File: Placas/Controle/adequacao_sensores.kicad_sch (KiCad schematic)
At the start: 2 parts, among them U1 LM324

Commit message: Adição de circuitos opcionais para PWM
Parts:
- C1: footprint Capacitor_THT:C_Disc_D8.0mm_W5.0mm_P7.50mm -> Capacitor_SMD:C_0805_2012Metric_Pad1.18x1.45mm_HandSolder
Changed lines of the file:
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@@
 		(dnp no)
 		(fields_autoplaced yes)
-		(property "Reference" "#PWR9"
+		(property "Reference" "#PWR11"
 			(at 184.15 49.53 0)
 			(effects
@@
 			(project "board"
 				(path "/01568b53-f202-4f02-9c1a-9c10c7610b4b/64ed1ee1-6201-4cd1-840c-b46b599d55ab"
-					(reference "#PWR9")
+					(reference "#PWR11")
 					(unit 1)
 				)
@@
 			)
 		)
-		(property "Footprint" "Capacitor_THT:C_Disc_D8.0mm_W5.0mm_P7.50mm"
+		(property "Footprint" "Capacitor_SMD:C_0805_2012Metric_Pad1.18x1.45mm_HandSolder"
 			(at 199.0852 49.53 0)
 			(effects
@@
 		(dnp no)
 		(fields_autoplaced yes)
-		(property "Reference" "#PWR8"
+		(property "Reference" "#PWR10"
 			(at 184.15 41.91 0)
 			(effects
@@
 			(project "board"
 				(path "/01568b53-f202-4f02-9c1a-9c10c7610b4b/64ed1ee1-6201-4cd1-840c-b46b599d55ab"
-					(reference "#PWR8")
+					(reference "#PWR10")
 					(unit 1)
 				)
@@
 			)
 		)
-		(property "C_sensor" "0,1u"
+		(property "C_sensor_1" "0,1u"
+			(at 41.91 50.8 0)
+			(effects
+				(font
+					(size 1.27 1.27)
+				)
+				(hide yes)
+			)
+		)
+		(property "C_sensor_2" "4,7u"
 			(at 41.91 50.8 0)
 			(effects
@@
 			)
 		)
-		(property "C_sensor" "0,1u"
+		(property "C_sensor_1" "0,1u"
 			(at 41.91 21.59 0)
 			(effects
+				(font
+					(size 1.27 1.27)
+				)
+				(hide yes)
+			)
+		)
+		(property "C_sensor_2" "4,7u"
+			(at 41.91 21.59 0)
+			(effects

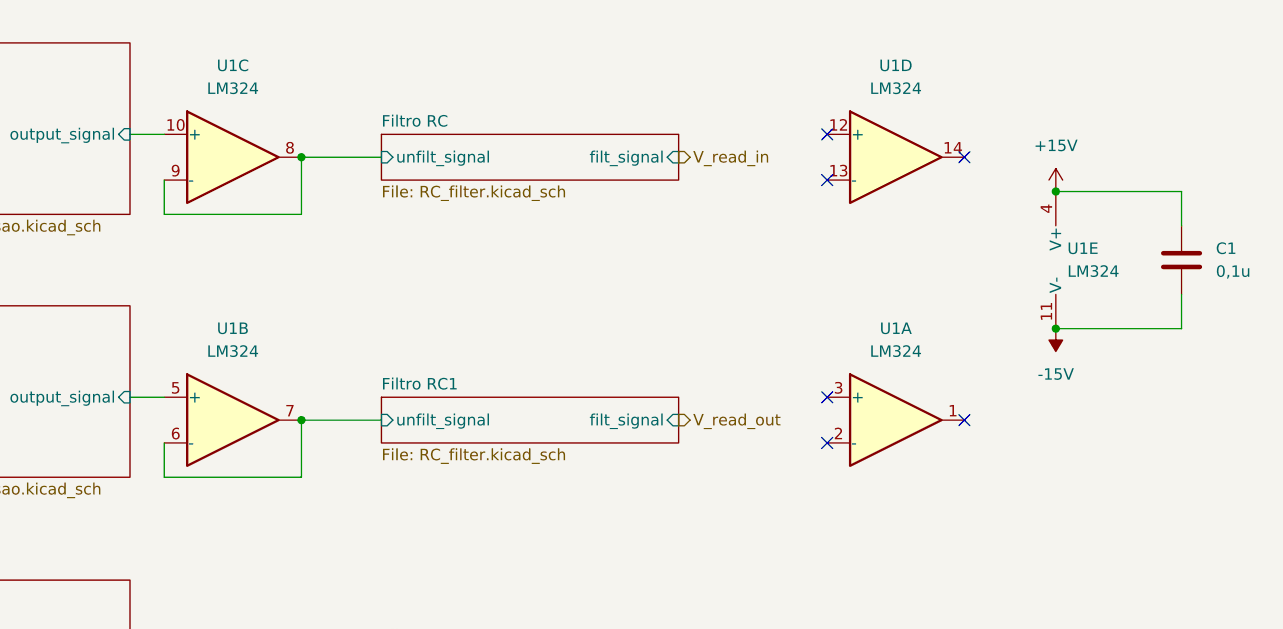
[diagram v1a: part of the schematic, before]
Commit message: Modificações nas duas placas, adição de furos para montagem, melhora na posição dos micros e conectores para comunicação SPI
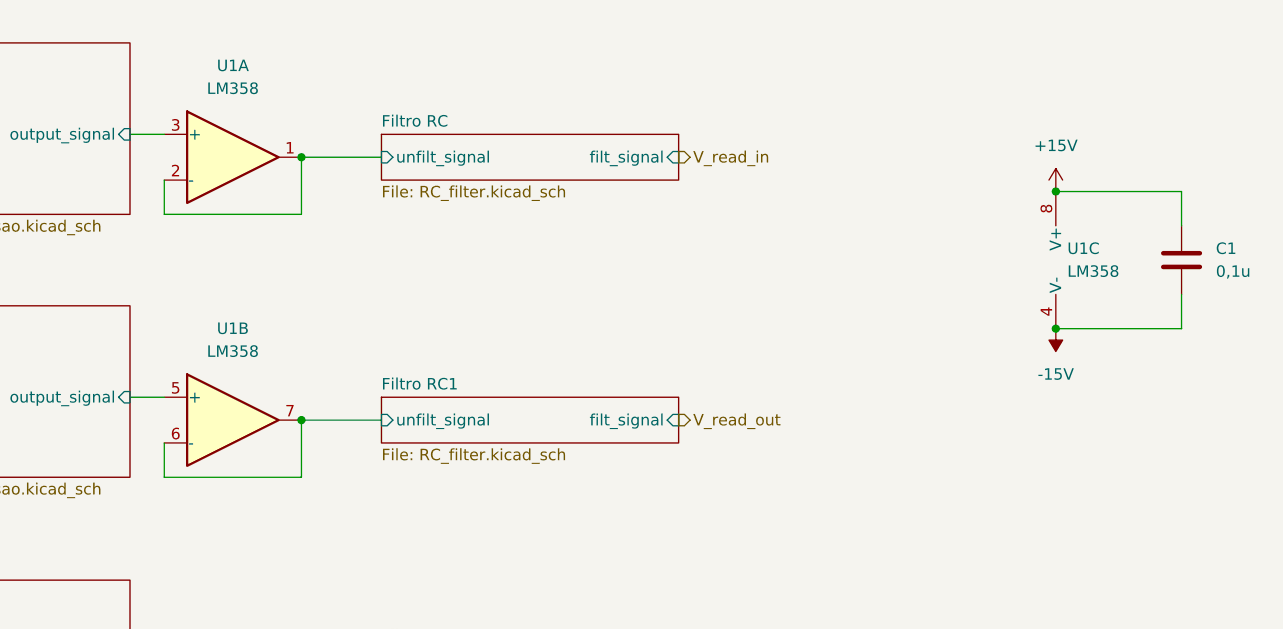
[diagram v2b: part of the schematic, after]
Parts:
- removed U1: LM324, Package_DIP:DIP-14_W7.62mm, symbol Amplifier_Operational:LM324
- added U1: LM358, Package_DIP:DIP-8_W7.62mm, symbol Amplifier_Operational:LM358
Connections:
- net +15V: now also U1.8 (V+)
- net -15V: now also U1.4 (V-)
- net Filtro RC/unfilt_signal: now also U1.1, U1.2 (-)
- net Filtro RC1/unfilt_signal: now also U1.6 (-), U1.7
- net adequacao_sensor_tensao/output_signal: now also U1.3 (+)
- net adequacao_sensor_tensao1/output_signal: now also U1.5 (+)
- no-connect marks 6 -> 0
